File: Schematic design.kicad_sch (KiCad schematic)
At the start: 58 parts, among them J2 Conn_01x05, J3 USB_C_Receptacle_USB2.0_16P, J4 Conn_01x02, U1 MAX30102, U2 MPU-6050, U3 LIS3MDL, U4 TLV61070ADBV, U5 TPS7A0518PDBV, U6 TPS7A0533PDBV, U7 MDBT50Q-1MV2, U8 MCP73831-2-OT, Y1 32.768kHz (6pF)

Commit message: Add files via upload
I noticed when making my bill of materials (BOM) that the MPU6050 and MAX30105 were discontinued/obsolete. Luckily, the MAX30105, MAX30102, and MAX30101 all have the same blueprint. However, only the MAX30101 and MAX30105 have the green light, which is optimal for sensing heartbeat. Even better, the MAX30101 and MAX30105 are electrically the same. The difference lies in the internal firmware, but the MAX30101 is actually better for a wearable anyways.

For the MPU6050, I selected the similar MPU6500, but had to install a library and symbol from SnapEDA. I then just rewired it appropriately based on the datasheet.

I then noticed a logical problem while reviewing the circuit: the I2C logic for the MAX30101 was running on 1.8V logic (max 2V), whereas the rest of the circuit modules could safely handle 3.3V, which is the micro-controller logic voltage. Because of this, I had to integrate a voltage translator into the system. This was to allow for proper I2C communication, while also ensuring the I2C pull-up resistors did not make the current in the I2C go over 3mA, as per I2C standards. I selected a PCA9306DCUR for this.
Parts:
- removed C6: 0.1uF, symbol Device:C
- removed U2: MPU-6050, Sensor_Motion:InvenSense_QFN-24_4x4mm_P0.5mm, symbol Sensor_Motion:MPU-6050
- added C36: 0.1uF, symbol Device:C
- added C37, C38: 100pF, symbol Device:C_Small
- added R11: 200K, symbol Device:R
- added R12, R13: 4.7K, symbol Device:R
- added U2: PCA9306DCUR, Package_SO:VSSOP-8_2.3x2mm_P0.5mm, symbol Interface:PCA9306DC1
- added U9: MPU-6500, MPU-6500:QFN40P300X300X95-25N, symbol MPU-6500:MPU-6500
- C8: value 10nF -> 0.1uF
- J2: value Conn_01x05 -> MOLEX 53261-0571
- J3: value USB_C_Receptacle_USB2.0_16P -> USB4105-GF-A
- J4: value Conn_01x02 -> MOLEX 51021-0200
- U1: value MAX30102 -> MAX30101
- Y1: value 32.768kHz (6pF) -> FC-135R 32.7680KA-E3
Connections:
- net GND: now also C7.2, C36.2, C37.2, C38.2, U9.11 (FSYNC), U9.18 (GND), U9.20 (RESV_2), U9.25 (EXP), U9.9 (AD0/SDO); no longer C7.1
- net MPU_int: now also U9.12 (INT)
- net SCL: now also C10.1, C11.1, C14.1, C15.1, C23.2, C24.2, C30.1, C34.1, C5.1, C8.2, J2.1 (Pin_1), R10.1, R9.2, U3.10 (~{CS}), U3.5 (Vdd), U3.6 (Vdd_IO), U6.5 (OUT), U7.22 (P0.06), U7.28 (VDD), U7.30 (VDDH), R11.1, R12.1, R13.1, U9.13 (VDD), U9.22 (NCS), U9.23 (SCL/SCLK), U9.24 (SDA/SDI), U9.8 (VDDIO); no longer R2.1, U1.2 (SCL)
- net Vdd_1.8V: now reaches C29.1, C3.1, C33.1, C4.1, U1.11 (VDD), U5.5 (OUT)
- net Vdd_1.8V: now also R1.2, R2.2, R3.2, C36.1, C37.1, U2.2 (VREF1)
- net at U3.11 (SDA/SDI/SDO): now also U9.21 (AUX_DA)
- net at U3.1 (SCL/SPC): now also U9.7 (AUX_CL)
- net SDA renamed SDA_HS
- net SDA_HS: now also U2.4 (SDA1); no longer U7.22 (P0.06)
- removed net Vdd_3.3v: C10.1, C11.1, C14.1, C15.1, C23.2, C24.2, C30.1, C34.1, C5.1, J2.1 (Pin_1), R1.2, R10.1, R2.2, R3.2, R9.2, U3.10 (~{CS}), U3.5 (Vdd), U3.6 (Vdd_IO), U6.5 (OUT), U7.28 (VDD)
- new net: C7.1, U9.10 (REGOUT)
- new net: R13.2, U2.5 (SDA2)
- new net: R12.2, U2.6 (SCL2)
- new net: C38.1, R11.2, U2.7 (VREF2), U2.8 (EN)
- new net SCL_HS: R2.1, U1.2 (SCL), U2.3 (SCL1)
- no-connect marks 44 -> 43
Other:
- note added: "Microcontroller"
- note added: "Voltage translator 1.8V t o 3.3V (I2C)"
- moved on the sheet: C14, C16, C17, C18, C19, C20, C21, C22, C23, C24, C26, C30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

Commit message: Add files via upload
I noticed I did not connect the pull-up resistors on the Voltage translator (3.3v side) properly. it is connected properly now. I also gave all the elements a footprint and a name for the BOM.
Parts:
- removed C14: 0.1uF, symbol Device:C
- C1, C13, C22, C23: value 10uF -> 10uF 10V; footprint (none) -> Capacitor_SMD:C_0603_1608Metric
- C10, C15, C2, C20, C21, C24, C25, C26, C27, C32, C33, C34, C35, C36, C4, C7, C8: value 0.1uF -> 0.1uF 10V; footprint (none) -> Capacitor_SMD:C_0402_1005Metric
- C11: value 1uF -> 1uF 10V; footprint (none) -> Capacitor_SMD:C_0402_1005Metric
- C12, C18, C19, C3: value 4.7uF -> 4.7uF 10V; footprint (none) -> Capacitor_SMD:C_0603_1608Metric
- C16, C17: value 6.8pF -> 6.8pF 50V C0G; footprint (none) -> Capacitor_SMD:C_0402_1005Metric
- C28, C29, C30, C31: value 1uF -> 1uF 10V; footprint (none) -> Capacitor_SMD:C_0603_1608Metric
- C37, C38: value 100pF -> 100pF 10V; footprint (none) -> Capacitor_SMD:C_0402_1005Metric
- C5: value 10nF -> 10nF 10V; footprint (none) -> Capacitor_SMD:C_0402_1005Metric
- C9: value 100nF -> 0.1uF 10V; footprint (none) -> Capacitor_SMD:C_0402_1005Metric
- R1, R2, R3: value 1k -> 1k 1%; footprint (none) -> Resistor_SMD:R_0402_1005Metric
- R10, R9: value 10k -> 10k 1%; footprint (none) -> Resistor_SMD:R_0402_1005Metric
- R11: value 200K -> 200K 1%; footprint (none) -> Resistor_SMD:R_0402_1005Metric
- R12, R13: value 4.7K -> 4.7K 1%; footprint (none) -> Resistor_SMD:R_0402_1005Metric
- R4: value 90.9K -> 90.9K 1%; footprint (none) -> Resistor_SMD:R_0402_1005Metric
- R5: value 10K -> 10K 1%; footprint (none) -> Resistor_SMD:R_0402_1005Metric
- R6, R7: value 5.11K -> 5.11K 1%; footprint (none) -> Resistor_SMD:R_0402_1005Metric
- R8: value 3.16K -> 3.16K 1%; footprint (none) -> Resistor_SMD:R_0402_1005Metric
- U9: footprint MPU-6500:QFN40P300X300X95-25N -> MPU-6500 footprint:QFN40P300X300X95-25N
- VCTA32251B-2R2MS6: renamed from L1; value 1.0uH -> 2.2uH; footprint (none) -> Inductor_SMD:L_1210_3225Metric
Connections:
- net GND: now also U2.1 (GND)
- net SCL: now also R12.2, U2.6 (SCL2); no longer C10.1, C11.1, C15.1, C23.2, C24.2, C30.1, C34.1, C5.1, C8.2, J2.1 (Pin_1), R10.1, R11.1, R12.1, R13.1, R9.2, U3.10 (~{CS}), U3.5 (Vdd), U3.6 (Vdd_IO), U6.5 (OUT), U7.22 (P0.06), U7.28 (VDD), U7.30 (VDDH), U9.13 (VDD), U9.22 (NCS), U9.24 (SDA/SDI), U9.8 (VDDIO)
- net SDA: now reaches R13.2, U2.5 (SDA2)
- net SDA: now also U7.22 (P0.06), U9.24 (SDA/SDI)
- new net Vdd_3.3v: C10.1, C11.1, C15.1, C23.2, C24.2, C30.1, C34.1, C5.1, C8.2, J2.1 (Pin_1), R10.1, R11.1, R12.1, R13.1, R9.2, U3.10 (~{CS}), U3.5 (Vdd), U3.6 (Vdd_IO), U6.5 (OUT), U7.28 (VDD), U7.30 (VDDH), U9.13 (VDD), U9.22 (NCS), U9.8 (VDDIO)
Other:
- moved on the sheet: R12, R13

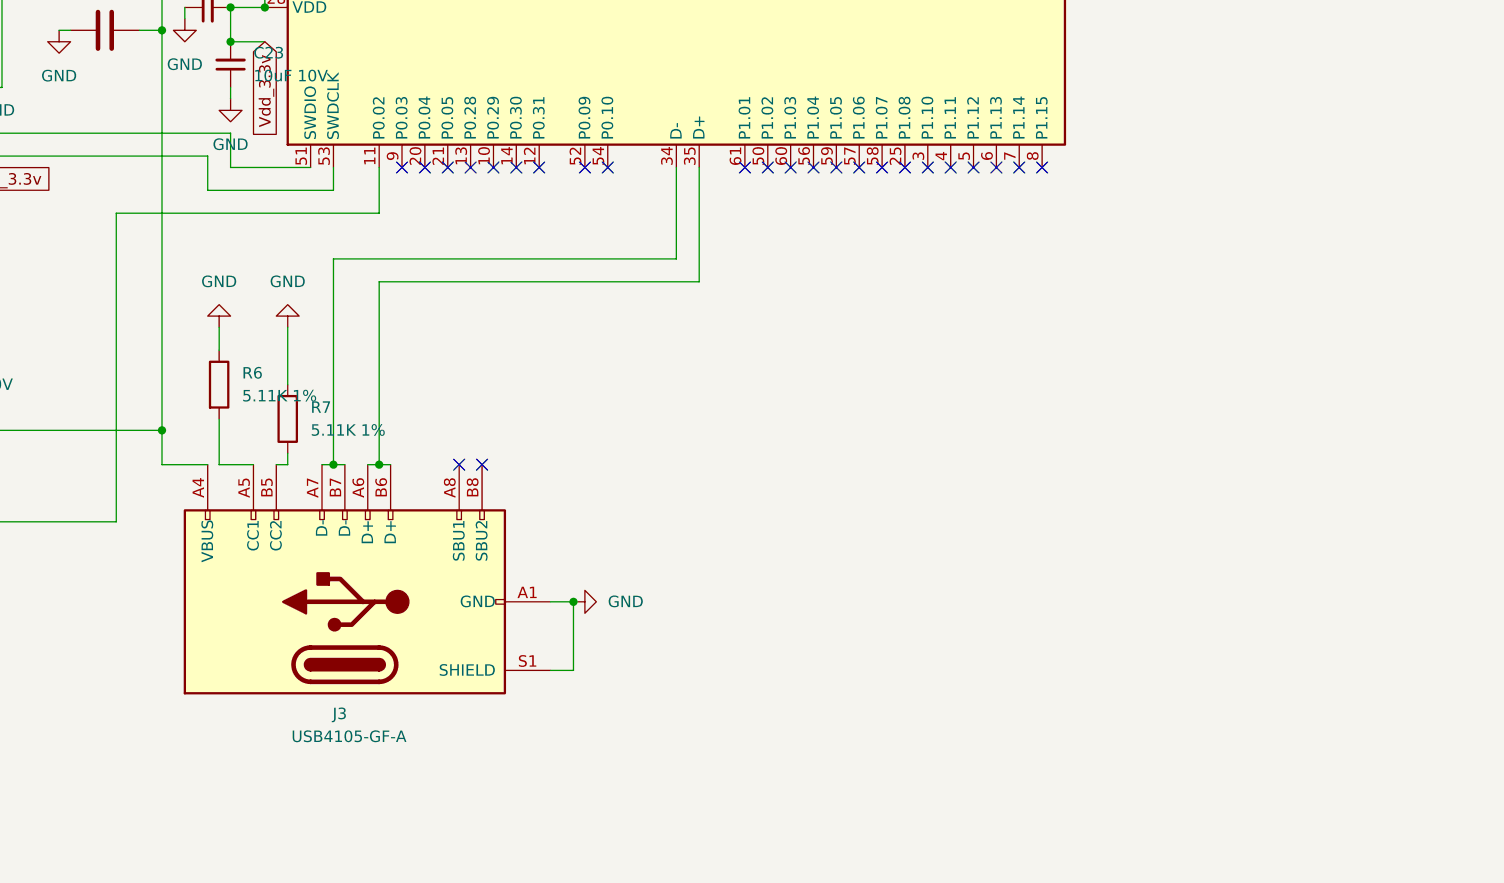
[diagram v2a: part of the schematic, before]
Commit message: Add files via upload
Added a USB Charging port protection IC (TPD4S014DSQR) in order to protect against low quality chargers or incompatible voltage chargers.
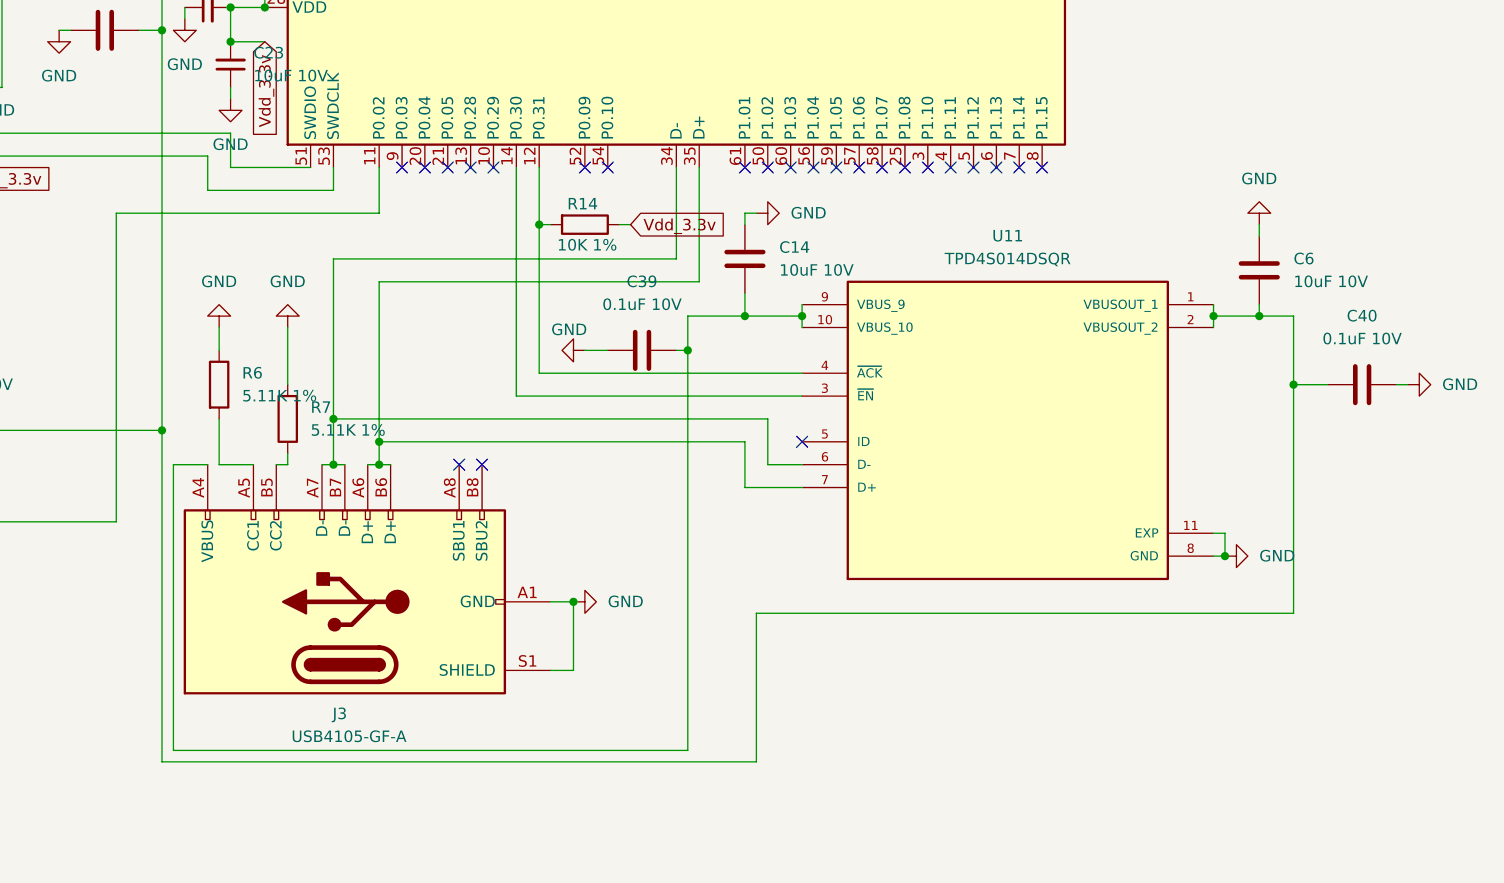
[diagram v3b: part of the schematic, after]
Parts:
- added C14, C6: 10uF 10V, Capacitor_SMD:C_0603_1608Metric, symbol Device:C
- added C39, C40: 0.1uF 10V, Capacitor_SMD:C_0402_1005Metric, symbol Device:C
- added R14: 10K 1%, Resistor_SMD:R_0402_1005Metric, symbol Device:R
- added U11: TPD4S014DSQR, TPD4S014DSQR Footprint:SON40P200X200X80-11N, symbol TPD4S014DSQR:TPD4S014DSQR
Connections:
- net GND: now also C14.2, C39.1, C40.2, C6.2, U11.11 (EXP), U11.8 (GND)
- net Vdd_3.3v: now also R14.1
- net at C18.2, C20.2, C21.2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: now also C40.1, C6.1, U11.1 (VBUSOUT_1), U11.2 (VBUSOUT_2); no longer J3.A4 (VBUS), J3.A9 (VBUS), J3.B4 (VBUS), J3.B9 (VBUS)
- net at U7.12 (P0.31): now also R14.2, U11.4 (~{ACK})
- net at U7.14 (P0.30): now also U11.3 (~{EN})
- net at J3.A7 (D-), J3.B7 (D-), U7.34 (D-): now also U11.6 (D-)
- net at J3.A6 (D+), J3.B6 (D+), U7.35 (D+): now also U11.7 (D+)
- new net: C14.1, C39.2, J3.A4 (VBUS), J3.A9 (VBUS), J3.B4 (VBUS), J3.B9 (VBUS), U11.10 (VBUS_10), U11.9 (VBUS_9)
- no-connect marks 43 -> 42

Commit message: Add files via upload
Final review before I start the PCB design. Systematically looked at every module 1 by 1 against its datasheet and caught some more mistakes I had made. I am truly confident in the circuit now and will start PCB routing.
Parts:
- removed C26: 0.1uF 10V, Capacitor_SMD:C_0402_1005Metric, symbol Device:C
- removed J3: USB4105-GF-A, Connector_USB:USB_C_Receptacle_GCT_USB4105-xx-A_16P_TopMnt_Horizontal, symbol Connector:USB_C_Receptacle_USB2.0_16P
- removed U8: MCP73831-2-OT, Package_TO_SOT_SMD:SOT-23-5, symbol Battery_Management:MCP73831-2-OT
- added C41, C42: 0.1uF 10V, Capacitor_SMD:C_0402_1005Metric, symbol Device:C
- added J1: USB4105-GF-A-120, USB4105-GF-A-120 footprint:GCT_USB4105-GF-A-120, symbol USB4105-GF-A-120:USB4105-GF-A-120
- added R15, R16: 4.7K 1%, Resistor_SMD:R_0402_1005Metric, symbol Device:R
- added R17, R18: 200K 1%, Resistor_SMD:R_0402_1005Metric, symbol Device:R
- added U10: MCP73832-2-OT, Package_TO_SOT_SMD:SOT-23-5, symbol Battery_Management:MCP73832-2-OT
- C16, C17: value 6.8pF 50V C0G -> 12pF 50V C0G
- Y1: value FC-135R 32.7680KA-E3 -> FC-135R 32.7680KA-AC3
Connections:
- net GND: now also C41.2, C42.2, J1.A1_B12 (GND), J1.B1_A12 (GND), J1.SH1 (SHELL_GND), J1.SH2 (SHELL_GND), J1.SH3 (SHELL_GND), J1.SH4 (SHELL_GND), R18.2, U10.2 (V_{SS})
- net VBat: now also C42.1, R17.2, U10.3 (V_{BAT})
- net Vdd_3.3v: now also C41.1, R15.2, R16.2
- net at C18.2, C20.2, C21.2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: now also U10.4 (V_{DD})
- net VBUS: now reaches C14.1, C39.2, U11.10 (VBUS_10), U11.9 (VBUS_9)
- net VBUS: now also J1.A4_B9 (VBUS), J1.B4_A9 (VBUS)
- net at R9.1, U7.11 (P0.02): now also U10.1 (STAT)
- net at U7.20 (P0.04): now also R17.1, R18.1
- net at U11.6 (D-), U7.34 (D-): now also J1.A7 (DN1), J1.B7 (DN2)
- net at U11.7 (D+), U7.35 (D+): now also J1.A6 (DP1), J1.B6 (DP2)
- net at R6.2: now also J1.A5 (CC1)
- net at R7.1: now also J1.B5 (CC2)
- net at U3.11 (SDA/SDI/SDO), U9.21 (AUX_DA): now also R16.1
- net at U3.1 (SCL/SPC), U9.7 (AUX_CL): now also R15.1
- net at R8.2: now also U10.5 (PROG)
- no-connect marks 42 -> 41
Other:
- moved on the sheet: C1, C10, C11, C12, C13, C14, C19, C2, C25, C28, C29, C3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
